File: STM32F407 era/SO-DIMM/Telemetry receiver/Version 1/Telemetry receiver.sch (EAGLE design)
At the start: 26 parts, among them Q2 12MHz, U7 LoPy

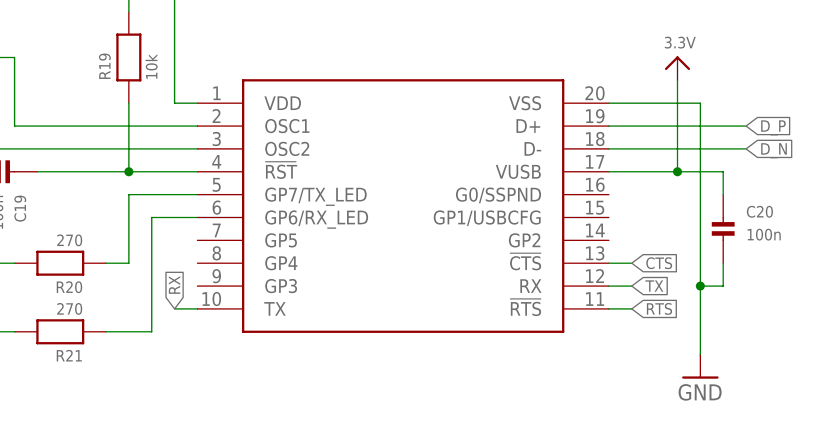
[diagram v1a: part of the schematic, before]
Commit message: last end changes on boards
Dev board
- Added 8 LED for ekstra debugging feature
- fixed Tvalue silkscreen
-

COM/TC
- fixed connections om P-channel RPP
- 12V from debug changed to include RPP and fuse

Dash
- fixed connections om P-channel RPP
- 12V from debug changed to include RPP and fuse

debug
- Added "ohm/not ohm to silkscreen
- Added BNC connectors for CAN

and much much more
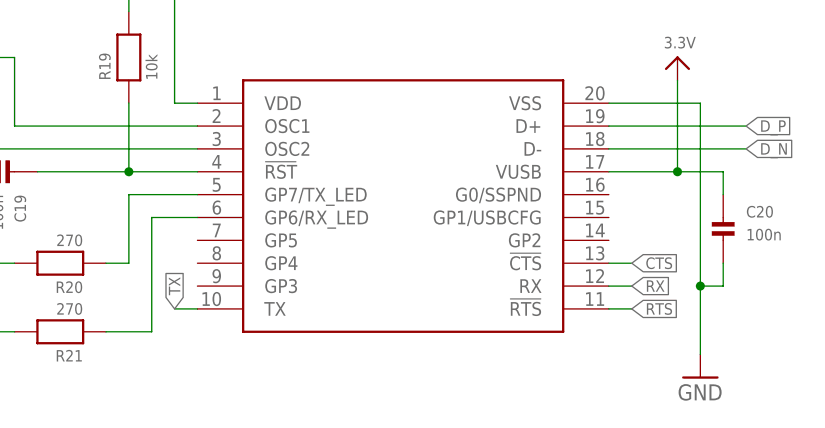
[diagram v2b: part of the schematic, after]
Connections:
- net RX: now also U$24.RX; no longer U$24.TX
- net TX: now also U$24.TX; no longer U$24.RX
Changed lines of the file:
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@@
 <net name="RX" class="0">
-<segment>
-<pinref part="U$24" gate="G$1" pin="TX"/>
-<wire x1="78.74" y1="96.52" x2="81.28" y2="96.52" width="0.1524" layer="91"/>
-<label x="78.74" y="96.52" size="1.27" layer="95" rot="R90" xref="yes"/>
-</segment>
 <segment>
 <label x="111.76" y="205.74" size="1.27" layer="95" rot="R180" xref="yes"/>
@@
 <label x="15.24" y="228.6" size="1.27" layer="95" rot="R180" xref="yes"/>
 </segment>
-</net>
-<net name="TX" class="0">
 <segment>
 <pinref part="U$24" gate="G$1" pin="RX"/>
@@
 <label x="129.54" y="99.06" size="1.27" layer="95" xref="yes"/>
 </segment>
+</net>
+<net name="TX" class="0">
 <segment>
 <pinref part="XB1" gate="G$1" pin="DIN/!CONFIG"/>
@@
 <label x="15.24" y="231.14" size="1.27" layer="95" rot="R180" xref="yes"/>
 </segment>
+<segment>
+<pinref part="U$24" gate="G$1" pin="TX"/>
+<wire x1="78.74" y1="96.52" x2="81.28" y2="96.52" width="0.1524" layer="91"/>
+<label x="78.74" y="96.52" size="1.27" layer="95" rot="R90" xref="yes"/>
+</segment>
 </net>

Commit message: error corrections
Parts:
- added R2: 499, microbuilder:RESISTOR_0603
- added R3: 976, microbuilder:RESISTOR_0603
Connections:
- new net N$7: R2.1, U7.P1/TX
- net 3.3V: no longer U7.3,3V
- net GND: now also R3.1
- net RX: now also R2.2, R3.2; no longer U7.P1/TX
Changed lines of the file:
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@@
 <part name="H4" library="holes" deviceset="MOUNT-HOLE" device="3.0"/>
 <part name="U7" library="AAU-Racing" deviceset="LOPY" device="" value="LoPy"/>
-<part name="U$15" library="microbuilder" deviceset="3.3V" device=""/>
 <part name="GND30" library="supply1" deviceset="GND" device=""/>
 <part name="U$16" library="microbuilder" deviceset="5.0V" device=""/>
@@
 <part name="LED1" library="microbuilder" deviceset="LED" device="1206"/>
 <part name="R1" library="microbuilder" deviceset="RESISTOR" device="_0603" value="500"/>
+<part name="R2" library="microbuilder" deviceset="RESISTOR" device="_0603" value="499"/>
+<part name="R3" library="microbuilder" deviceset="RESISTOR" device="_0603" value="976"/>
+<part name="GND3" library="supply1" deviceset="GND" device=""/>
 </parts>
 <sheets>
@@
 <instance part="H4" gate="G$1" x="-86.36" y="139.7"/>
 <instance part="U7" gate="G$1" x="27.94" y="210.82"/>
-<instance part="U$15" gate="G$1" x="30.48" y="251.46"/>
 <instance part="GND30" gate="1" x="27.94" y="182.88"/>
 <instance part="U$16" gate="G$1" x="25.4" y="251.46"/>
@@
 <instance part="LED1" gate="G$1" x="106.68" y="213.36" rot="MR0"/>
 <instance part="R1" gate="G$1" x="96.52" y="205.74" rot="R270"/>
+<instance part="R2" gate="G$1" x="7.62" y="228.6" rot="R180"/>
+<instance part="R3" gate="G$1" x="0" y="220.98" rot="R90"/>
+<instance part="GND3" gate="1" x="0" y="213.36"/>
 </instances>
 <busses>
@@
 <wire x1="-43.18" y1="180.34" x2="-43.18" y2="177.8" width="0.1524" layer="91"/>
 </segment>
+<segment>
+<pinref part="R3" gate="G$1" pin="1"/>
+<pinref part="GND3" gate="1" pin="GND"/>
+</segment>
 </net>
 <net name="3.3V" class="0">
@@
 <wire x1="30.48" y1="119.38" x2="30.48" y2="121.92" width="0.1524" layer="91"/>
 <junction x="30.48" y="121.92"/>
-</segment>
-<segment>
-<pinref part="U7" gate="G$1" pin="3,3V"/>
-<pinref part="U$15" gate="G$1" pin="3.3V"/>
-<wire x1="30.48" y1="246.38" x2="30.48" y2="248.92" width="0.1524" layer="91"/>
 </segment>
 <segment>
@@
 </segment>
 <segment>
-<pinref part="U7" gate="G$1" pin="P1/TX"/>
-<wire x1="15.24" y1="228.6" x2="17.78" y2="228.6" width="0.1524" layer="91"/>
-<label x="15.24" y="228.6" size="1.27" layer="95" rot="R180" xref="yes"/>
-</segment>
-<segment>
 <pinref part="U$24" gate="G$1" pin="RX"/>
 <wire x1="129.54" y1="99.06" x2="127" y2="99.06" width="0.1524" layer="91"/>
 <label x="129.54" y="99.06" size="1.27" layer="95" xref="yes"/>
+</segment>
+<segment>
+<pinref part="R2" gate="G$1" pin="2"/>
+<wire x1="-2.54" y1="228.6" x2="0" y2="228.6" width="0.1524" layer="91"/>
+<pinref part="R3" gate="G$1" pin="2"/>
+<wire x1="0" y1="228.6" x2="2.54" y2="228.6" width="0.1524" layer="91"/>
+<wire x1="0" y1="226.06" x2="0" y2="228.6" width="0.1524" layer="91"/>
+<junction x="0" y="228.6"/>
+<label x="-2.54" y="228.6" size="1.27" layer="95" rot="R180" xref="yes"/>
 </segment>
 </net>
@@
 </segment>
 </net>
+<net name="N$7" class="0">
+<segment>
+<pinref part="R2" gate="G$1" pin="1"/>
+<pinref part="U7" gate="G$1" pin="P1/TX"/>
+<wire x1="12.7" y1="228.6" x2="17.78" y2="228.6" width="0.1524" layer="91"/>
+</segment>
+</net>

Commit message: final changes
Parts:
- removed R2: 499, microbuilder:RESISTOR_0603
- removed R3: 976, microbuilder:RESISTOR_0603
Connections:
- removed net N$7: R2.1, U7.P1/TX
- net GND: no longer R3.1
- net RX: now also U7.P1/TX; no longer R2.2, R3.2
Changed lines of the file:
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@@
 <part name="LED1" library="microbuilder" deviceset="LED" device="1206"/>
 <part name="R1" library="microbuilder" deviceset="RESISTOR" device="_0603" value="500"/>
-<part name="R2" library="microbuilder" deviceset="RESISTOR" device="_0603" value="499"/>
-<part name="R3" library="microbuilder" deviceset="RESISTOR" device="_0603" value="976"/>
-<part name="GND3" library="supply1" deviceset="GND" device=""/>
 </parts>
 <sheets>
@@
 <instance part="LED1" gate="G$1" x="106.68" y="213.36" rot="MR0"/>
 <instance part="R1" gate="G$1" x="96.52" y="205.74" rot="R270"/>
-<instance part="R2" gate="G$1" x="7.62" y="228.6" rot="R180"/>
-<instance part="R3" gate="G$1" x="0" y="220.98" rot="R90"/>
-<instance part="GND3" gate="1" x="0" y="213.36"/>
 </instances>
 <busses>
@@
 <wire x1="-43.18" y1="180.34" x2="-43.18" y2="177.8" width="0.1524" layer="91"/>
 </segment>
-<segment>
-<pinref part="R3" gate="G$1" pin="1"/>
-<pinref part="GND3" gate="1" pin="GND"/>
-</segment>
 </net>
 <net name="3.3V" class="0">
@@
 </segment>
 <segment>
-<pinref part="R2" gate="G$1" pin="2"/>
-<wire x1="-2.54" y1="228.6" x2="0" y2="228.6" width="0.1524" layer="91"/>
-<pinref part="R3" gate="G$1" pin="2"/>
-<wire x1="0" y1="228.6" x2="2.54" y2="228.6" width="0.1524" layer="91"/>
-<wire x1="0" y1="226.06" x2="0" y2="228.6" width="0.1524" layer="91"/>
-<junction x="0" y="228.6"/>
-<label x="-2.54" y="228.6" size="1.27" layer="95" rot="R180" xref="yes"/>
+<label x="15.24" y="228.6" size="1.27" layer="95" rot="R180" xref="yes"/>
+<pinref part="U7" gate="G$1" pin="P1/TX"/>
+<wire x1="17.78" y1="228.6" x2="15.24" y2="228.6" width="0.1524" layer="91"/>
 </segment>
 </net>
@@
 </segment>
 </net>
-<net name="N$7" class="0">
-<segment>
-<pinref part="R2" gate="G$1" pin="1"/>
-<pinref part="U7" gate="G$1" pin="P1/TX"/>
-<wire x1="12.7" y1="228.6" x2="17.78" y2="228.6" width="0.1524" layer="91"/>
-</segment>
-</net>

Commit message: BOM done
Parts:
- U2: value (none) -> 3,3v
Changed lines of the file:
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@@
 <part name="GND26" library="supply1" deviceset="GND" device=""/>
 <part name="C20" library="microbuilder" deviceset="CAP_CERAMIC" device="_0603" value="100n"/>
-<part name="U2" library="microbuilder" deviceset="LM1117" device="SOT223-REFLOW"/>
+<part name="U2" library="microbuilder" deviceset="LM1117" device="SOT223-REFLOW" value="3,3v"/>
 <part name="U$1" library="microbuilder" deviceset="3.3V" device=""/>
 <part name="GND2" library="supply1" deviceset="GND" device=""/>
